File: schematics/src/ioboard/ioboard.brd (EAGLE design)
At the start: 35.6 x 99.1 mm, 32 parts, among them IC1 TL072P, IC2 TL072P, IC3 TL072P

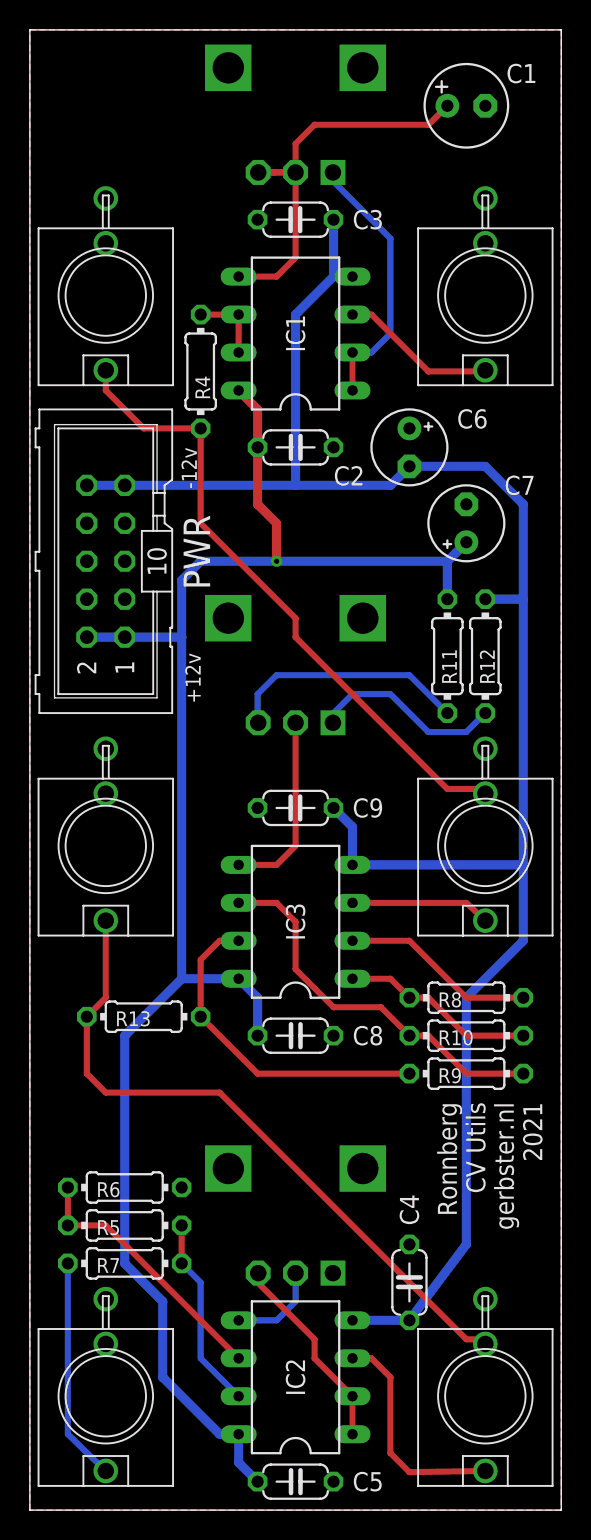
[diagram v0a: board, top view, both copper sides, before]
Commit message: Updated Schematics, Fixed Power Socket orientation
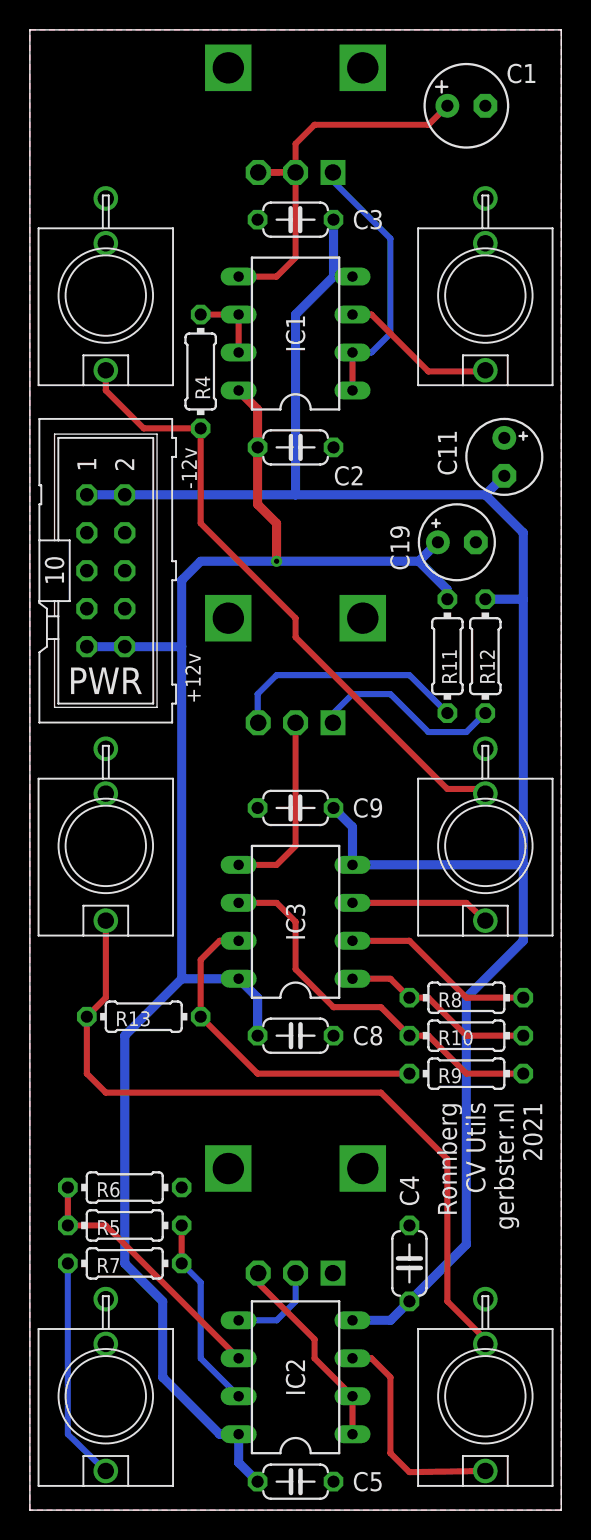
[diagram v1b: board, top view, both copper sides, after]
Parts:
- removed C6, C7: 10uf, resistor:E2,5-5
- added C11, C19: 10uf, resistor:E2,5-5
- moved C4 1.27 mm to (25.4, 16.5)
- moved PWR 0.63 mm to (5.08, 62.9), turned to 270 degrees
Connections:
- net +12V: now also C19.+, PWR.10, PWR.9; no longer C7.+, PWR.1, PWR.2
- net -12V: now also C11.-, PWR.1, PWR.2; no longer C6.-, PWR.10, PWR.9
- net GND: now also C11.+, C19.-; no longer C6.+, C7.-
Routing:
- net IO_OFFSET_OUT: track 45.1 -> 50.7 mm
- net +12V: track 115.9 -> 114.8 mm
